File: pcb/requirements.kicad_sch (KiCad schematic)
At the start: 0 parts

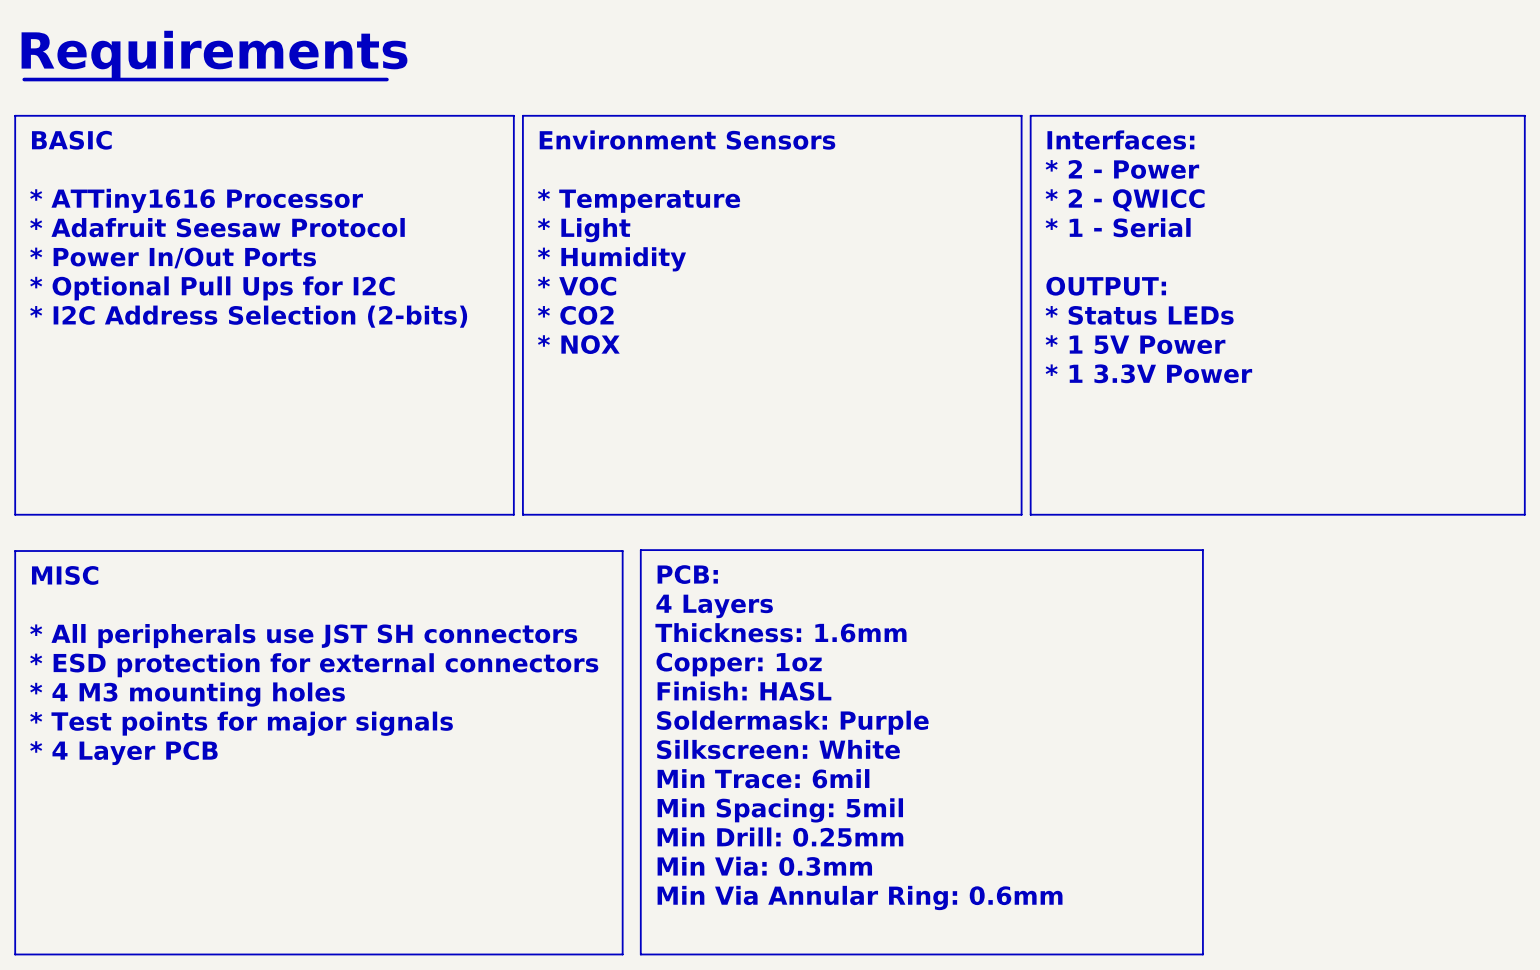
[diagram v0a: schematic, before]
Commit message: Updated license and implemented RP2040
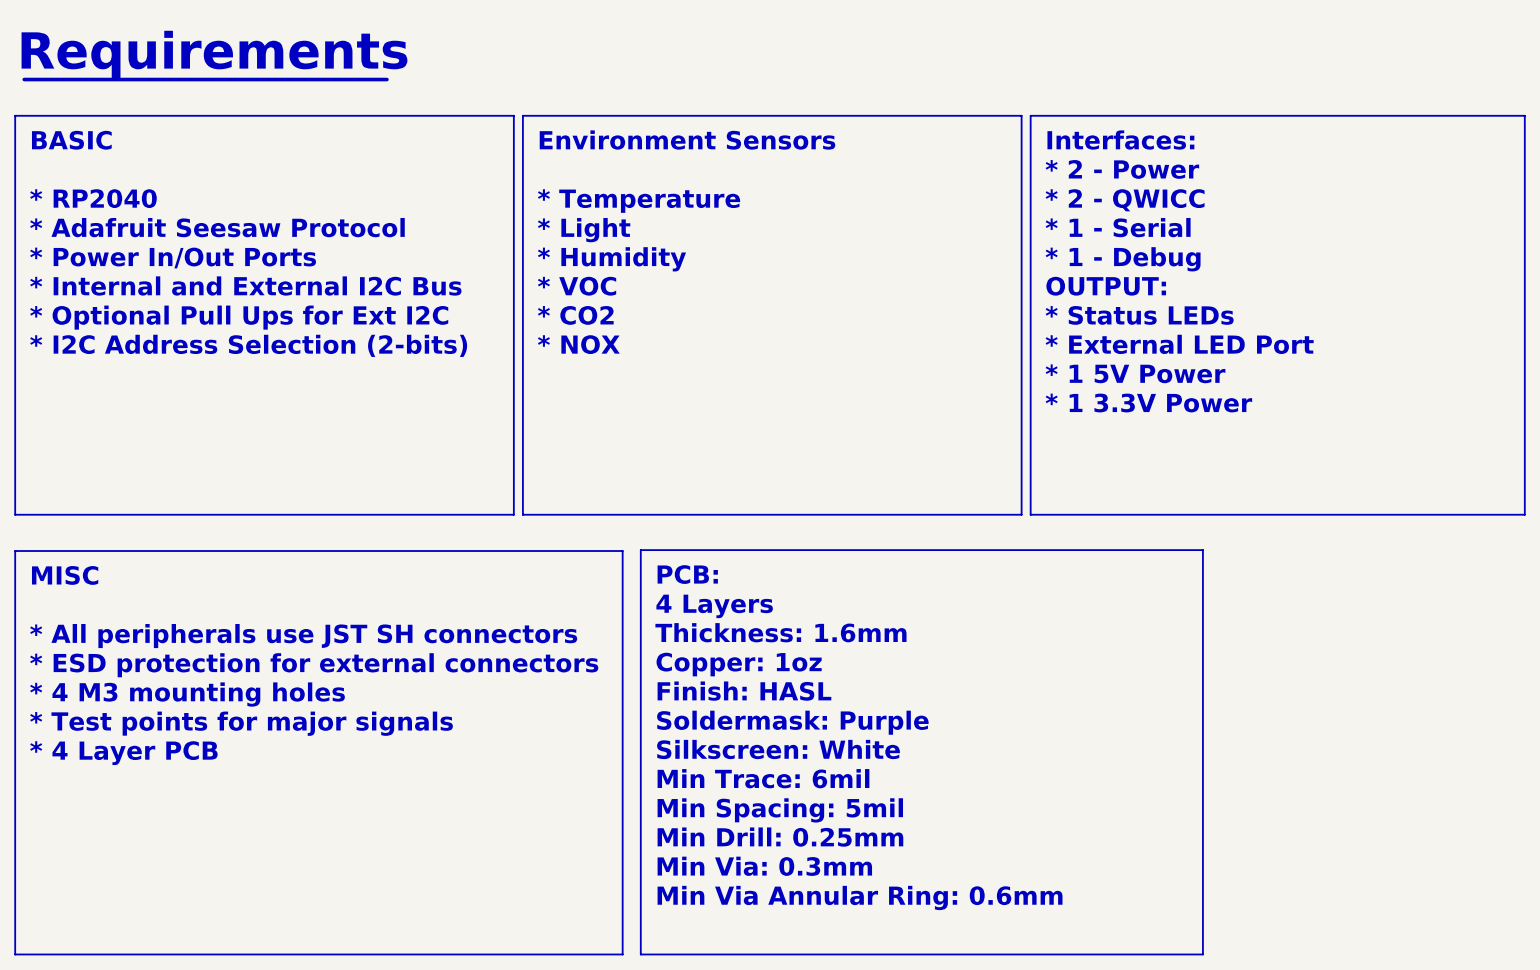
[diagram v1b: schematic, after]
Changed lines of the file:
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@@
 		)
 	)
-	(text_box "BASIC\n\n* ATTiny1616 Processor\n* Adafruit Seesaw Protocol\n* Power In/Out Ports\n* Optional Pull Ups for I2C\n* I2C Address Selection (2-bits)"
+	(text_box "BASIC\n\n* RP2040\n* Adafruit Seesaw Protocol\n* Power In/Out Ports\n* Internal and External I2C Bus\n* Optional Pull Ups for Ext I2C\n* I2C Address Selection (2-bits)\n"
 		(exclude_from_sim yes)
 		(at 19.05 32.385 0)
@@
 		)
 	)
-	(text_box "Interfaces:\n* 2 - Power\n* 2 - QWICC\n* 1 - Serial\n\nOUTPUT:\n* Status LEDs\n* 1 5V Power\n* 1 3.3V Power"
+	(text_box "Interfaces:\n* 2 - Power\n* 2 - QWICC\n* 1 - Serial\n* 1 - Debug\nOUTPUT:\n* Status LEDs\n* External LED Port\n* 1 5V Power\n* 1 3.3V Power"
 		(exclude_from_sim yes)
 		(at 161.29 32.385 0)
